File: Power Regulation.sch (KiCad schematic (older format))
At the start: 10 parts, among them P401 CONN_01X02, P402 CONN_01X02, U401 LD1117S12TR, U402 LD1117S33TR

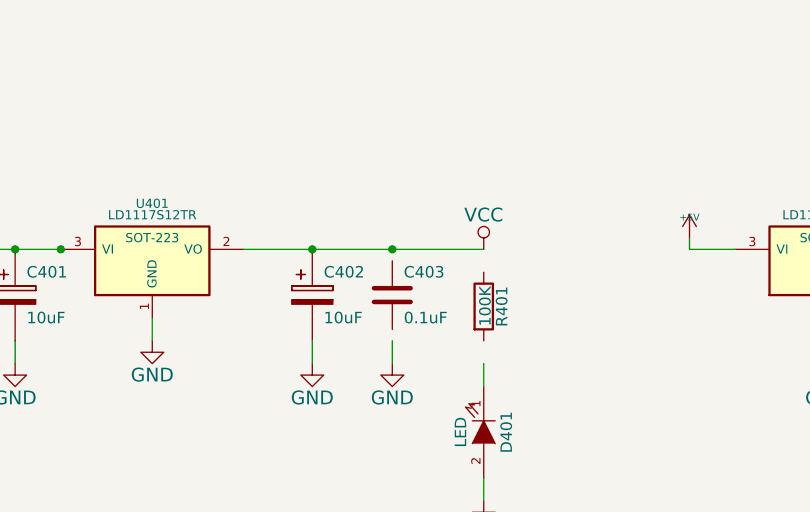
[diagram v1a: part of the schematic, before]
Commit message: Issue #4 RAW goes through LDO, +5v from USB doesn't
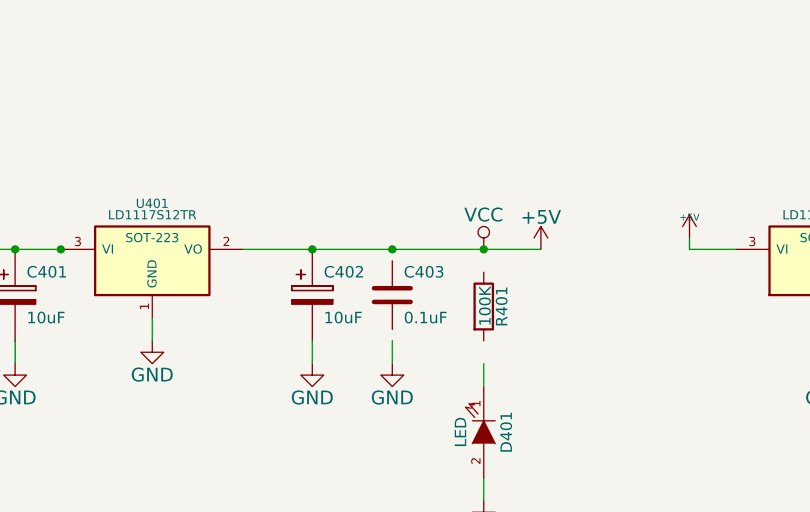
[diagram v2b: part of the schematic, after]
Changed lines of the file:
@@
 $EndComp
 Wire Wire Line
-	5550 2100 6600 2100
+	5550 2100 6850 2100
 Wire Wire Line
 	4250 2100 4750 2100
@@
 	1    0    0    -1
 $EndComp
+$Comp
+L +5V #PWR?
+U 1 1 55911069
+P 6850 2100
+F 0 "#PWR?" H 6850 1950 60  0001 C CNN
+F 1 "+5V" H 6850 2240 60  0000 C CNN
+F 2 "" H 6850 2100 60  0000 C CNN
+F 3 "" H 6850 2100 60  0000 C CNN
+	1    6850 2100
+	1    0    0    -1
+$EndComp
+Connection ~ 6600 2100
 $EndSCHEMATC

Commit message: Version 0.2
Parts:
- C401, C402: footprint (none) -> Capacitors_SMD:c_elec_4x5.8
- C403: footprint (none) -> Capacitors_SMD:C_0805; symbol C -> C-RESCUE-espduino
- D401: footprint (none) -> LEDs:LED-0805; symbol LED -> LED-RESCUE-espduino
- P401, P402: footprint (none) -> Pin_Headers:Pin_Header_Straight_1x02
- R401: footprint (none) -> Resistors_SMD:R_0805_HandSoldering; symbol R -> R-RESCUE-espduino
- U401, U402: footprint SOT-223 -> SMD_Packages:SOT-223
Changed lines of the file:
@@
 EESchema Schematic File Version 2
+LIBS:espduino-rescue
 LIBS:power
 LIBS:device
@@
 LIBS:memory
 LIBS:xilinx
-LIBS:special
 LIBS:microcontrollers
 LIBS:dsp
@@
 LIBS:valves
 LIBS:littlebush
+LIBS:ab2_7segment
+LIBS:ab2_audio
+LIBS:ab2_buffer
+LIBS:ab2_capacitor
+LIBS:ab2_connectivity
+LIBS:ab2_dac
+LIBS:ab2_diode
+LIBS:ab2_gpio_expansion
+LIBS:ab2_header
+LIBS:ab2_idc
+LIBS:ab2_inductor
+LIBS:ab2_input_devices
+LIBS:ab2_jumper
+LIBS:ab2_lcd
+LIBS:ab2_led
+LIBS:ab2_opamp
+LIBS:ab2_pot
+LIBS:ab2_power
+LIBS:ab2_regulator
+LIBS:ab2_relay
+LIBS:ab2_resistor
+LIBS:ab2_sensor
+LIBS:ab2_stepper
+LIBS:ab2_supply
+LIBS:ab2_terminal_block
+LIBS:ab2_test
+LIBS:ab2_transistor
+LIBS:ab2_uC
+LIBS:ab2_usb
+LIBS:ab2_xtal
 LIBS:espduino-cache
 EELAYER 25 0
@@
 $Descr A4 11693 8268
 encoding utf-8
-Sheet 4 5
+Sheet 4 6
 Title ""
 Date ""
@@
 F 0 "U402" H 8100 2400 40  0000 C CNN
 F 1 "LD1117S33TR" H 8100 2350 40  0000 C CNN
-F 2 "SOT-223" H 8100 2250 40  0000 C CNN
+F 2 "SMD_Packages:SOT-223" H 8100 2250 40  0000 C CNN
 F 3 "" H 8100 2150 60  0000 C CNN
 	1    8100 2150
@@
 $EndComp
 $Comp
-L LED D401
+L LED-RESCUE-espduino D401
 U 1 1 5534E48F
 P 6600 2900
 F 0 "D401" H 6600 3000 50  0000 C CNN
 F 1 "LED" H 6600 2800 50  0000 C CNN
-F 2 "" H 6600 2900 60  0000 C CNN
+F 2 "LEDs:LED-0805" H 6600 2900 60  0001 C CNN
 F 3 "" H 6600 2900 60  0000 C CNN
 	1    6600 2900
@@
 $EndComp
 $Comp
-L R R401
+L R-RESCUE-espduino R401
 U 1 1 5534E496
 P 6600 2350
 F 0 "R401" V 6680 2350 50  0000 C CNN
 F 1 "100K" V 6607 2351 50  0000 C CNN
-F 2 "" V 6530 2350 30  0000 C CNN
+F 2 "Resistors_SMD:R_0805_HandSoldering" V 6530 2350 30  0001 C CNN
 F 3 "" H 6600 2350 30  0000 C CNN
 	1    6600 2350
@@
 $EndComp
 $Comp
-L C C403
+L C-RESCUE-espduino C403
 U 1 1 5534E49D
 P 6200 2300
 F 0 "C403" H 6250 2400 50  0000 L CNN
 F 1 "0.1uF" H 6250 2200 50  0000 L CNN
-F 2 "" H 6238 2150 30  0000 C CNN
+F 2 "Capacitors_SMD:C_0805" H 6238 2150 30  0001 C CNN
 F 3 "" H 6200 2300 60  0000 C CNN
 	1    6200 2300
@@
 F 0 "C402" H 5900 2400 50  0000 L CNN
 F 1 "10uF" H 5900 2200 50  0000 L CNN
-F 2 "" H 5888 2150 30  0000 C CNN
+F 2 "Capacitors_SMD:c_elec_4x5.8" H 5888 2150 30  0001 C CNN
 F 3 "" H 5850 2300 60  0000 C CNN
 	1    5850 2300
@@
 F 0 "C401" H 4600 2400 50  0000 L CNN
 F 1 "10uF" H 4600 2200 50  0000 L CNN
-F 2 "" H 4588 2150 30  0000 C CNN
+F 2 "Capacitors_SMD:c_elec_4x5.8" H 4588 2150 30  0001 C CNN
 F 3 "" H 4550 2300 60  0000 C CNN
 	1    4550 2300
@@
 F 0 "U401" H 5150 2400 40  0000 C CNN
 F 1 "LD1117S12TR" H 5150 2350 40  0000 C CNN
-F 2 "SOT-223" H 5150 2250 40  0000 C CNN
+F 2 "SMD_Packages:SOT-223" H 5150 2250 40  0000 C CNN
 F 3 "" H 5150 2150 60  0000 C CNN
 	1    5150 2150
@@
 F 0 "P401" H 1600 1500 50  0000 C CNN
 F 1 "CONN_01X02" V 1750 1300 50  0000 C CNN
-F 2 "" H 1600 1350 60  0000 C CNN
+F 2 "Pin_Headers:Pin_Header_Straight_1x02" H 1600 1350 60  0001 C CNN
 F 3 "" H 1600 1350 60  0000 C CNN
 	1    1600 1350
@@
 F 0 "P402" H 1600 2400 50  0000 C CNN
 F 1 "CONN_01X02" V 1750 2200 50  0000 C CNN
-F 2 "" H 1600 2250 60  0000 C CNN
+F 2 "Pin_Headers:Pin_Header_Straight_1x02" H 1600 2250 60  0001 C CNN
 F 3 "" H 1600 2250 60  0000 C CNN
 	1    1600 2250
